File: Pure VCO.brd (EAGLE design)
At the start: 48.8 x 100 mm, 76 parts, among them T1 TRANS_PAIR, T2 N_CHN, U1 QUAD_OPAMP, U2 QUAD_OPAMP, U3 DUAL_OPAMP

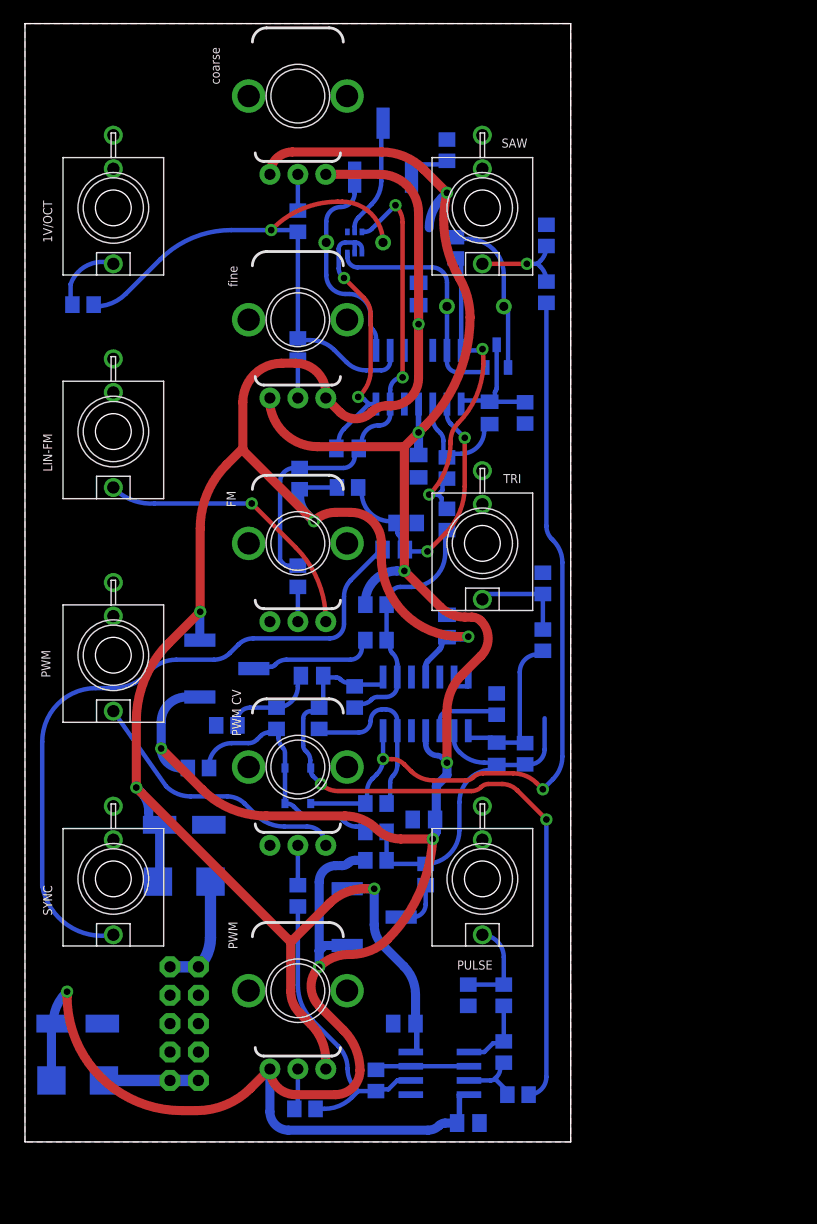
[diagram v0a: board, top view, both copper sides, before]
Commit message: VCO 2.1
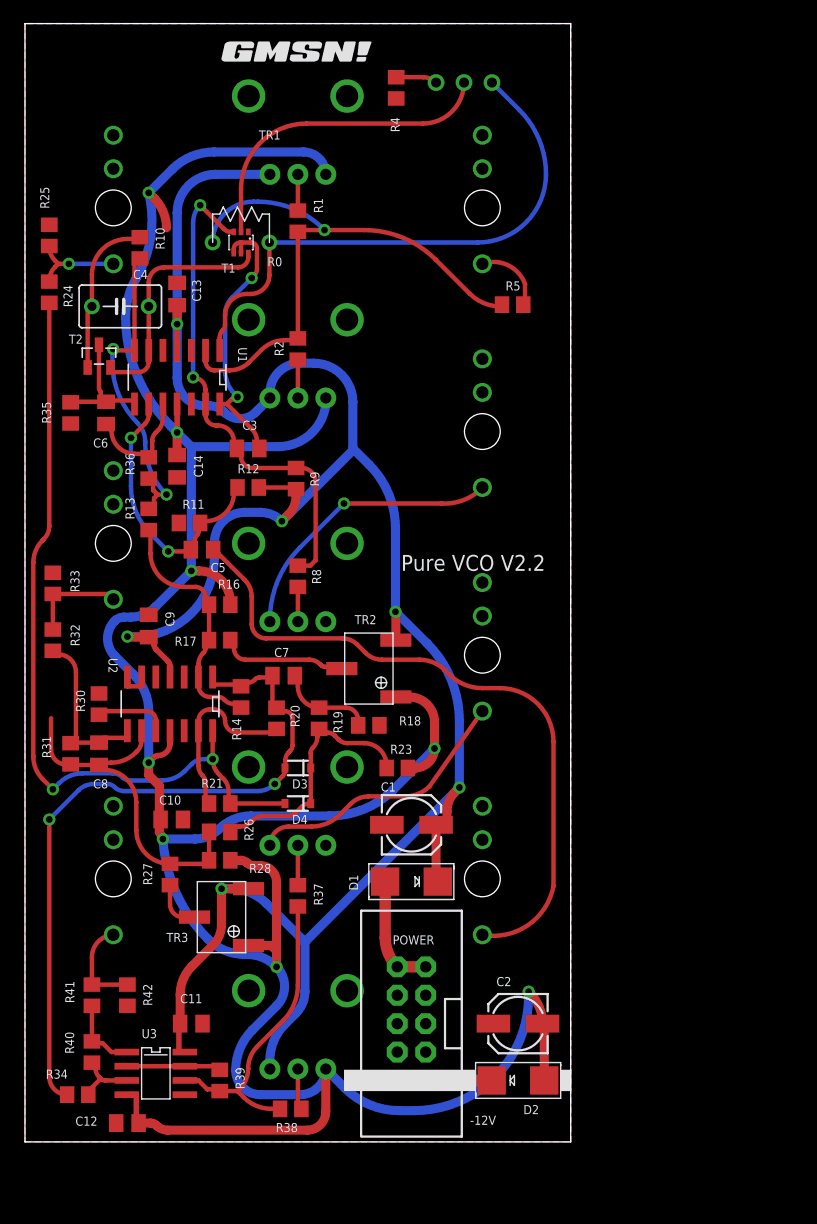
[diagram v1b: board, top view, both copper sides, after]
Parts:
- removed 2M, 2M1, 2M4, 2M5: 2K2, rcl:R0805
- removed 2M3: 120K, rcl:R0805
- removed 3K1: 9K1, rcl:R0805
- removed 3K3: 15K, rcl:R0805
- added R35, R41: 3K3, rcl:R0805
- added R36: 9K1, rcl:R0805
- added R38: 120K, rcl:R0805
- added R39: 100K, rcl:R0805
- added R40: 2M, rcl:R0805
- added R42: 1K5, rcl:R0805
- added U$1, U$2: (no value), gmsnLogo:GMSN!_LOGO
- R23: value 19K -> 19k1
- TR1: device INSTRUO:TRIM_3269W -> INSTRUO:TRIMMER_TH3
- moved R24 44.5 mm to (3.17, 92.7), flipped to the top
- moved R25 44.5 mm to (3.17, 97.8), flipped to the top
- moved R32 43.8 mm to (3.49, 61.6), flipped to the top
- moved R33 43.8 mm to (3.49, 66.7), flipped to the top
- moved R31 40.6 mm to (5.08, 51.4), flipped to the top
- moved C2 39.4 mm to (45.1, 27.3), flipped to the top
- moved D2 39.4 mm to (45.1, 22.2), flipped to the top
- moved R34 39.4 mm to (5.71, 21.0), flipped to the top
- moved R5 38.4 mm to (44.6, 91.6), flipped to the top
- moved C8 35.6 mm to (7.62, 51.4), flipped to the top
- moved R30 35.6 mm to (7.62, 55.9), flipped to the top
- moved T2 35.6 mm to (7.62, 87.0), flipped to the top
- moved C6 34.3 mm to (8.26, 81.9), flipped to the top
- moved 1V/OCT 33.0 mm to (41.9, 100.2), flipped to the bottom
- moved LIN-FM 33.0 mm to (41.9, 80.2), flipped to the bottom
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- renumbered 2M2 to R37
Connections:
- net GND: now also R35.1, R42.1; no longer 2M5.1, 3K3.1
- net N$16: now also R36.2; no longer 3K1.2
- net N$19: now also R36.1; no longer 3K1.1
- net N$20: now also R35.2; no longer 3K3.2
- net N$36: now also R40.1; no longer 2M.1
- net N$39: now also R40.2, R41.2; no longer 2M.2, 2M4.2
- net N$40: now also R38.1; no longer 2M3.1
- net N$42: now also R38.2, R39.1; no longer 2M1.1, 2M3.2
- net N$43: now also R39.2; no longer 2M1.2
- net N$44: now also R41.1, R42.2; no longer 2M4.1, 2M5.2
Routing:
- net N$7: track 18.5 -> 48.5 mm
- net N$10: track 10.5 -> 27.7 mm
- net N$8: track 4.36 -> 3.66 mm
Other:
- board text added: "Pure VCO V2.2"
- board text added: "copyright GMSN Ltd 2016"

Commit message: VCO 2.3
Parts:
- removed 1V/OCT, LIN-FM, PULSE, PWM, SAW, SYNC, TRI: (no value), INSTRUO:S_JACK
- removed COARSE, FINE, FM_ATT, PWM_ATT, PWM_POT: B100K, INSTRUO:Q-POT
- removed R0: 2K, INSTRUO:RESISTOR_TC
- removed T2: N_CHN, INSTRUO:N_CHN
- removed U2: QUAD_OPAMP, INSTRUO:QUAD_OPAMP
- removed U3: DUAL_OPAMP, INSTRUO:DUAL_OPAMP
- added C15, C16, C18, C19: 100n, GMSN:C0805K
- added C17: 100p, GMSN:C0805K
- added CP1, CP2: 10u, GMSN:153CLV-0505
- added IC1, IC2, IC3, IC4, IC5, IC6: TL072D, GMSN:SO08
- added J1, J2, J3, J4, J5, J6, J7, J8: S_JACK, GMSN:S_JACK
- added R15: 56K, GMSN:R0805
- added R22: 1K5, GMSN:R0805
- added R29: 2K, GMSN:R0805
- added R3: 100K, GMSN:R0805
- added R43, R44, R46: 10K, GMSN:R0805
- added R45: empty, GMSN:R0805
- added R47: 1K3, GMSN:R0805
- added R6: 390R, GMSN:R0805
- added R7: 87k, GMSN:R0805
- added TC1: 2K, GMSN:RESISTOR_TC
- added TP1, TP2: TRANS_PAIR, GMSN:TRANS_PAIR
- added TR4, TR5: 100K, GMSN:TRIMMER_TH3
- added VR1: Coarse, GMSN:POT
- added VR2, VR3, VR4, VR5: B100K, GMSN:POT
- C1, C2: value (none) -> 100n; device rcl:153CLV-0505 -> GMSN:C0805K
- C10, C11, C12, C3, C9: device rcl:C0805K -> GMSN:C0805K
- C13: value 100n -> 10nF; device rcl:C0805K -> GMSN:C0805K
- C14: value 100n -> 1000p; device rcl:C0805K -> GMSN:C0805K
- C4: value 2.2n -> 100p; device INSTRUO:POLY_CAP -> GMSN:C0805K
- C5: value 100p -> 100n; device rcl:C0805K -> GMSN:C0805K
- C6: value 22p -> 100n; device rcl:C0805K -> GMSN:C0805K
- C7: value 10nF -> 2.2n; device rcl:C0805K -> GMSN:POLY_CAP
- C8: value 1000p -> 22p; device rcl:C0805K -> GMSN:C0805K
- D1, D2: device adafruit:SMADIODE -> GMSN:SMADIODE
- D3, D4: device SparkFun-DiscreteSemi:SOD-323 -> GMSN:SOD-323F
- R1, R2: device rcl:R0805 -> GMSN:R0805
- R10: value 680R -> 39K; device rcl:R0805 -> GMSN:R0805
- R11: value 15K -> 680R; device rcl:R0805 -> GMSN:R0805
- R12: value 22K -> 9K1; device rcl:R0805 -> GMSN:R0805
- R13: value 10K -> 5K6; device rcl:R0805 -> GMSN:R0805
- R14: value 39K -> 10K; device rcl:R0805 -> GMSN:R0805
- R16: value 56K -> 100K; device rcl:R0805 -> GMSN:R0805
- R17: value 5K6 -> 39K; device rcl:R0805 -> GMSN:R0805
- R18: value 10K -> 2K2; device rcl:R0805 -> GMSN:R0805
- R19: value 10K -> 2M; device rcl:R0805 -> GMSN:R0805
- R20: value 22K* -> 10K; device rcl:R0805 -> GMSN:R0805
- R21: value 22K* -> 3K3; device rcl:R0805 -> GMSN:R0805
- R23: value 19k1 -> 10K; device rcl:R0805 -> GMSN:R0805
- R24, R25: value 2K -> 22K*; device rcl:R0805 -> GMSN:R0805
- R26: value 10K -> 19k1; device rcl:R0805 -> GMSN:R0805
- R27: value 100K -> 2K; device rcl:R0805 -> GMSN:R0805
- R28: value 27K -> 10K; device rcl:R0805 -> GMSN:R0805
- R30: value * -> 100K; device rcl:R0805 -> GMSN:R0805
- R31: value 10K -> 27K; device rcl:R0805 -> GMSN:R0805
- R32: value 1K3 -> 10K; device rcl:R0805 -> GMSN:R0805
- R33: value 2K -> 1K3; device rcl:R0805 -> GMSN:R0805
- R34: value 2K2 -> 2K; device rcl:R0805 -> GMSN:R0805
- R35: value 3K3 -> 1K3; device rcl:R0805 -> GMSN:R0805
- R36: value 9K1 -> 3K3; device rcl:R0805 -> GMSN:R0805
- R37: value 39K -> 2K; device rcl:R0805 -> GMSN:R0805
- R38: value 120K -> 10K; device rcl:R0805 -> GMSN:R0805
- R39: value 100K -> 402R; device rcl:R0805 -> GMSN:R0805
- R4: value 390R -> 2M; device rcl:R0805 -> GMSN:R0805
- R40: value 2M -> 10K; device rcl:R0805 -> GMSN:R0805
- R41: value 3K3 -> 10K; device rcl:R0805 -> GMSN:R0805
- R42: value 1K5 -> 2K; device rcl:R0805 -> GMSN:R0805
- R5: value 100K -> 560K; device rcl:R0805 -> GMSN:R0805
- R8: value 560K -> 3K3; device rcl:R0805 -> GMSN:R0805
- R9: value 2M -> 120K; device rcl:R0805 -> GMSN:R0805
- T1: value TRANS_PAIR -> N_CHN; device INSTRUO:TRANS_PAIR -> GMSN:N_CHN
- TR1: device INSTRUO:TRIMMER_TH3 -> GMSN:TRIMMER_TH3
- TR2, TR3: device INSTRUO:TRIM_3269W -> GMSN:TRIMMER_TH3
- U1: value QUAD_OPAMP -> LM4040A50IDBZT; device INSTRUO:QUAD_OPAMP -> GMSN:SOT95P237X112-3N
- moved U$1 95.7 mm to (41.1, 19.7)
- moved C2 75.2 mm to (15.4, 96.4)
- moved C12 65.3 mm to (11.2, 83.7)
- moved C1 64.3 mm to (5.08, 101.7), turned to 180 degrees
- moved C8 62.1 mm to (46.7, 99.7)
- moved R10 53.1 mm to (26.0, 45.7), turned to 0 degrees
- moved R9 50.0 mm to (24.8, 26.0), turned to 180 degrees
- moved C11 48.5 mm to (7.87, 75.2)
- moved C10 47.6 mm to (42.4, 83.9), turned to 0 degrees
- moved C4 47.3 mm to (37.8, 53.5), turned to 0 degrees
- moved R8 42.9 mm to (46.6, 104.6), turned to 180 degrees
- moved C5 42.5 mm to (41.5, 104.3)
- moved R27 41.4 mm to (3.43, 80.6), turned to 180 degrees
- moved C7 40.5 mm to (39.6, 95.9), flipped to the bottom, turned to 180 degrees
- moved D2 37.1 mm to (30.4, 56.3), turned to 90 degrees
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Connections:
- removed net N$25: C7.1, D3.2, R14.1, R20.2, R34.1, U2.1OUT
- removed net N$35: R30.2, U2.3+IN
- removed net N$38: R32.1, R33.1, TRI.TIP
- removed net N$43: R39.2, U3.-1IN, U3.2OUT
- removed net N$45: U2.2-IN, U2.2OUT
- new net N$14: C17.1, IC6.2, R38.2, R44.2, TP2.C2
- new net N$6: IC3.1, IC3.6, R16.2
- new net N$75: IC5.7, R47.1, TR4.1, TR4.2
- new net N$76: R37.1, TP2.B2, TR4.3
- new net N$77: R39.1, TP2.E2, TR5.1
- new net N$78: R39.2, TP2.E1, TR5.3
- new net N$79: R40.1, TR5.2
- new net N$80: R42.1, TP2.B1
- new net N$82: IC6.3, R41.2, R43.1, TP2.C1
- new net N$83: IC5.5, R35.1, R36.1
- new net N$84: IC6.6, R45.2, R46.2
- new net PULSEIN: C13.1, D3.A, IC4.1, R17.1, R18.1, R24.2
- new net SAWCORE: IC2.1, R11.1, R12.1, R14.2
- new net SINE: IC6.7, J8.TIP, R46.1
- new net SINE_PRE1: C17.2, IC6.1, IC6.5, R44.1
- new net TRI: J7.TIP, R33.1, R34.1, R35.2
- net +12V: now also C1.1, C15.1, C18.1, C5.1, CP1.+, IC1.8, IC2.8, IC3.8, IC4.8, IC5.8, IC6.8, R38.1, R4.2, R41.1, R7.2, VR1.P$3, VR2.P$3, VR4.P$3; no longer C1.+, C13.1, COARSE.P$3, FINE.P$3, PWM_POT.P$3, R12.2, R9.2, U1.VCC++, U2.VCC++, U3.+VCC
- net -12V: now also C16.2, C19.2, C2.2, C6.2, CP2.-, IC1.4, IC2.4, IC3.4, IC4.4, IC5.4, IC6.4, R15.2, R26.2, R31.1, R40.2, VR1.P$1, VR2.P$1, VR4.P$1; no longer C14.2, C2.-, COARSE.P$1, FINE.P$1, PWM_POT.P$1, R16.2, R23.2, R28.1, U1.VCC--, U2.VCC--, U3.-VCC
- net GND: now also C1.2, C15.2, C16.1, C18.2, C19.1, C2.1, C5.2, C6.1, CP1.-, CP2.+, IC1.3, IC1.5, IC2.3, IC3.3, IC4.3, IC4.5, IC5.3, J1.GND, J1.NORM, J2.GND, J2.NORM, J3.GND, J4.GND, J5.GND, J6.GND, J7.GND, J8.GND, R20.2, R22.1, R29.2, R34.2, R36.2, R37.2, R42.2, R43.2, R45.1, R6.1, R8.1, TP1.B1, U1.2, VR3.P$1, VR5.P$1; no longer 1V/OCT.GND, 1V/OCT.NORM, C1.-, C13.2, C14.1, C2.+, FM_ATT.P$1, LIN-FM.GND, LIN-FM.NORM, PULSE.GND, PWM.GND, PWM_ATT.P$1, R11.1, R18.2, R25.2, R30.1, R33.2, R35.1, R4.1, R42.1, SAW.GND, SYNC.GND, T1.B2, TRI.GND, U1.1+IN, U1.2+IN, U1.4+IN, U2.1+IN, U2.2+IN, U2.4+IN, U3.+2IN
- net N$10: now also TP1.B2; no longer T1.B1
- net N$11: now also C7.2, R11.2, T1.D; no longer C4.2, R10.2, T2.D
- net N$12: now also IC1.6, R4.1, R5.1, TP1.C2; no longer R8.1, R9.1, T1.C1, U1.4-IN
- net N$13: now also C7.1, IC2.2, T1.S, TP1.C1; no longer C4.1, T1.C2, T2.S, U1.2-IN
- net N$15: now also J1.TIP, VR3.P$3; no longer FM_ATT.P$3, LIN-FM.TIP
- net N$16: now also C8.1, IC2.5, R12.2; no longer C6.1, R36.2, U1.3+IN
- net N$17: now also R5.2, VR3.P$2; no longer FM_ATT.P$2, R8.2
- net N$18: now also IC1.7, TP1.E1, TP1.E2; no longer T1.E1, T1.E2, U1.4OUT
- net N$19: now also IC5.6, R47.2; no longer R10.1, R13.2, R36.1, U1.2OUT
- net N$2: now also VR1.P$2; no longer COARSE.P$2
- net N$20: now also C8.2, IC2.7, R8.2, T1.G; no longer C6.2, R35.2, T2.G, U1.3OUT
- net N$21: now also C4.1, J3.TIP; no longer C5.1, SYNC.TIP
- net N$22: now also C4.2, IC2.6, R7.1, U1.1; no longer C5.2, R11.2, R12.1, U1.3-IN
- net N$23: now also R13.1; no longer R17.1
- net N$24: now also IC4.2, R13.2, R14.1, R15.1; no longer R13.1, R14.2, R16.1, U2.1-IN
- net N$27: now also J6.TIP, R27.1, R29.1; no longer R24.1, R25.1, SAW.TIP
- net N$28: now also C13.2, R20.1, R23.1; no longer C7.2, R18.1, R19.1
- net N$29: now also R30.1; no longer R27.1
- net N$30: now also IC4.6, R24.1, R25.2; no longer R20.1, R21.2, U2.4-IN
- net N$31: now also D4.A, IC4.7, R25.1, R27.2; no longer D4.2, R21.1, R24.2, U2.4OUT
- net N$33: now also D3.C, D4.C, R23.2, R28.1; no longer D3.1, D4.1, R19.2, R23.1
- net N$34: now also C14.1, IC5.2, R30.2, R32.2; no longer C8.1, R26.2, R27.2, U2.3-IN
- net N$36: now also IC3.5, R18.2, R19.1; no longer R34.2, R40.1, U3.+1IN
- net N$37: now also C14.2, IC5.1, R32.1, R33.2; no longer C8.2, R31.1, R32.2, U2.3OUT
- net N$39: now also IC3.7, R19.2, R21.2; no longer R40.2, R41.2, U3.1OUT
- net N$4: now also IC1.2, R3.1, TC1.1; no longer R0.1, R5.1, U1.1-IN
- net N$40: now also R9.1, VR4.P$2; no longer PWM_POT.P$2, R38.1
- net N$41: now also J4.TIP, VR5.P$3; no longer PWM.TIP, PWM_ATT.P$3
- net N$42: now also IC3.2, R10.2, R16.1, R9.2; no longer R37.2, R38.2, R39.1, U3.-2IN
- net N$44: now also J5.TIP, R21.1, R22.2; no longer PULSE.TIP, R41.1, R42.2
- net N$46: now also R10.1, VR5.P$2; no longer PWM_ATT.P$2, R37.1
- net N$5: now also VR2.P$2; no longer FINE.P$2
- net N$7: now also IC1.1, TC1.2; no longer R0.2, U1.1OUT
- net N$8: now also R6.2; no longer R4.2
- net N$9: now also J2.TIP, R3.2; no longer 1V/OCT.TIP, R5.2
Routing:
- net +12V: track 199.5 -> 273.7 mm
- net N$25: track 64.5 -> 0.00 mm, vias 2 -> 0
- net N$31: track 71.5 -> 9.45 mm, vias 2 -> 0
- net N$21: track 59.2 -> 3.30 mm
- net N$42: track 27.5 -> 80.6 mm, vias 0 -> 2
- net N$14: track 0.00 -> 50.5 mm
- net N$75: track 0.00 -> 39.2 mm
- net PULSEIN: track 0.00 -> 37.6 mm
- net N$4: track 52.4 -> 84.4 mm, vias 1 -> 2
- net SAWCORE: track 0.00 -> 31.6 mm
- net N$22: track 24.2 -> 54.9 mm
- net N$13: track 21.5 -> 50.4 mm, vias 0 -> 1
- net -12V: track 259.0 -> 231.3 mm, vias 8 -> 7
- net N$82: track 0.00 -> 27.7 mm
- net N$7: track 48.5 -> 21.7 mm
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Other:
- board text added: "Pure VCO V3 cc-by 4.0 2017"
- board text removed: "-12V"
- board text removed: "FM"
- board text removed: "POWER"
- board text removed: "PWM"
- board text removed: "PWM CV"
- board text removed: "Pure VCO V2.2"
- board text removed: "T1"
- board text removed: "T2"
- board text removed: "TR1"
- board text removed: "TR2"
- board text removed: "TR3"
- board text removed: "coarse"
- board text removed: "copyright GMSN Ltd 2016"
- board text removed: "fine"

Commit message: VCO 3.0
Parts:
- removed J1, J2, J3, J4, J5, J6, J7, J8: S_JACK, GMSN:S_JACK
- removed U1: LM4040A50IDBZT, GMSN:SOT95P237X112-3N
- removed VR1: Coarse, GMSN:POT
- removed VR2, VR3, VR4, VR5: B100K, GMSN:POT
- added 1V/OCT, LIN, MIX, PULSE, PWM_IN, SAW, SINE, SYNC, TRI: PJ301M-12, GMSN:PJ301M-12
- added C20, C21: 100nF, GMSN:C0805
- added COARSE, FINE, FM_LEVEL, PULSE_MIX, PULSE_WIDTH, PWM_LEVEL, SAW_MIX, SINE_MIX, TRI_MIX: B100k, GMSN:POTENTIOMETER_9MM
- added IC7: TL072, GMSN:SO08
- added IC8: LM4040A50IDBZT, GMSN:SOT95P237X112-3N
- added R48, R49, R50, R51, R52, R53: 100k, GMSN:R0805
- C1, C10, C11, C12, C15, C16, C18, C19, C2, C5, C6, C9: value 100n -> 100nF; device GMSN:C0805K -> GMSN:C0805
- C13: device GMSN:C0805K -> GMSN:C0805
- C14: value 1000p -> 1nF; device GMSN:C0805K -> GMSN:C0805
- C17, C3, C4: value 100p -> 100pF; device GMSN:C0805K -> GMSN:C0805
- C7: value 2.2n -> 2.2nF
- C8: value 22p -> 22pF; device GMSN:C0805K -> GMSN:C0805
- CP1, CP2: value 10u -> 10uF
- D1, D2: value (none) -> STTH102A
- D3, D4: value (none) -> 1N914
- IC1, IC2, IC3, IC4, IC5, IC6: value TL072D -> TL072
- JP1: value M05X2SHD -> HEADER2X5SHD; device SparkFun-Connectors:2X5-SHROUDED -> GMSN:2X5-SHROUDED
- R1: value 150K -> 150k
- R10, R17: value 39K -> 39k
- R12: value 9K1 -> 9k1
- R13: value 5K6 -> 5k6
- R14, R20, R23, R28, R38, R40, R41, R43, R44: value 10K -> 10k
- R15: value 56K -> 56k
- R16, R3, R30: value 100K -> 100k
- R18: value 2K2 -> 2k2
- R21: value 3K3 -> 1k5
- R22: value 1K5 -> 1k5
- R24, R25: value 22K* -> 22k
- R27, R29, R34, R37, R42: value 2K -> 2k
- R31: value 27K -> 27k
- R32, R46: value 10K -> 19k1
- R33, R35, R47: value 1K3 -> 1k3
- R36, R8: value 3K3 -> 3k3
- R45: value empty -> 10k
- R5: value 560K -> 560k
- R9: value 120K -> 120k
- T1: value N_CHN -> MMBFJ309
- TC1: value 2K -> 2k; device GMSN:RESISTOR_TC -> GMSN:0204/7
- TP1, TP2: value TRANS_PAIR -> DMMT3904W-7-F
- TR1: device GMSN:TRIMMER_TH3 -> GMSN:TRIMMER_TH
- TR2, TR3, TR4, TR5: value 100K -> 100k; device GMSN:TRIMMER_TH3 -> GMSN:TRIMMER_TH
- moved U$1 68.9 mm to (51.5, 87.8), turned to 90 degrees
- moved R36 50.2 mm to (52.8, 54.1), turned to 0 degrees
- moved TR3 50.1 mm to (55.9, 57.8)
- moved R30 47.8 mm to (58.4, 39.2), turned to 270 degrees
- moved R47 47.7 mm to (52.5, 51.7), turned to 0 degrees
- moved C16 46.5 mm to (56.0, 43.8), turned to 270 degrees
- moved D1 46.5 mm to (50.8, 14.0), turned to 180 degrees
- moved R35 45.3 mm to (48.1, 54.1), turned to 180 degrees
- moved C4 45.0 mm to (67.0, 19.2)
- moved CP2 44.9 mm to (20.3, 19.1), turned to 0 degrees
- moved R31 44.5 mm to (56.1, 39.0), turned to 270 degrees
- moved D2 43.5 mm to (20.3, 14.0), turned to 180 degrees
- moved R44 43.4 mm to (18.5, 61.3)
- moved IC5 43.1 mm to (52.2, 46.2), turned to 0 degrees
- moved CP1 42.7 mm to (50.8, 19.1), turned to 0 degrees
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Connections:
- removed net N$27: J6.TIP, R27.1, R29.1
- new net N$25: IC7.6, IC7.7
- new net N$35: IC7.3, R48.2, R49.2, R50.2, R51.2
- new net N$38: R48.1, SAW_MIX.P$2
- new net N$43: R49.1, TRI_MIX.P$2
- new net N$45: R51.1, SINE_MIX.P$2
- new net N$48: IC7.2, R52.1, R53.2
- new net N$49: IC7.1, MIX.TIP, R52.2
- new net PULSE: PULSE.TIP, PULSE_MIX.P$3, R21.1, R22.2
- new net SAW: R27.1, R29.1, SAW.TIP, SAW_MIX.P$3
- net +12V: now also C20.1, COARSE.P$3, FINE.P$3, IC7.8, PULSE_WIDTH.P$3; no longer VR1.P$3, VR2.P$3, VR4.P$3
- net -12V: now also C21.2, COARSE.P$1, FINE.P$1, IC7.4, PULSE_WIDTH.P$1; no longer VR1.P$1, VR2.P$1, VR4.P$1
- net GND: now also 1V/OCT.GND, 1V/OCT.NORM, C20.2, C21.1, FM_LEVEL.P$1, IC7.5, IC8.2, LIN.GND, LIN.NORM, MIX.GND, PULSE.GND, PULSE_MIX.P$1, PWM_IN.GND, PWM_LEVEL.P$1, R53.1, SAW.GND, SAW_MIX.P$1, SINE.GND, SINE_MIX.P$1, SYNC.GND, TRI.GND, TRI_MIX.P$1; no longer J1.GND, J1.NORM, J2.GND, J2.NORM, J3.GND, J4.GND, J5.GND, J6.GND, J7.GND, J8.GND, U1.2, VR3.P$1, VR5.P$1
- net N$15: now also FM_LEVEL.P$3, LIN.TIP; no longer J1.TIP, VR3.P$3
- net N$17: now also FM_LEVEL.P$2; no longer VR3.P$2
- net N$2: now also COARSE.P$2; no longer VR1.P$2
- net N$21: now also SYNC.TIP; no longer J3.TIP
- net N$22: now also IC8.1; no longer U1.1
- net N$40: now also PULSE_WIDTH.P$2; no longer VR4.P$2
- net N$41: now also PWM_IN.TIP, PWM_LEVEL.P$3; no longer J4.TIP, VR5.P$3
- net N$44: now also PULSE_MIX.P$2, R50.1; no longer J5.TIP, R21.1, R22.2
- net N$46: now also PWM_LEVEL.P$2; no longer VR5.P$2
- net N$5: now also FINE.P$2; no longer VR2.P$2
- net N$9: now also 1V/OCT.TIP; no longer J2.TIP
- net SINE: now also SINE.TIP, SINE_MIX.P$3; no longer J8.TIP
- net TRI: now also TRI.TIP, TRI_MIX.P$3; no longer J7.TIP
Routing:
- net SAW: track 0.00 -> 146.8 mm
- net N$22: track 54.9 -> 159.9 mm
- net N$34: track 31.7 -> 108.8 mm
- net PULSE: track 0.00 -> 73.9 mm, vias 0 -> 1
- net N$35: track 0.00 -> 69.4 mm, vias 0 -> 4
- net -12V: track 231.3 -> 288.5 mm, vias 7 -> 9
- net +12V: track 273.7 -> 327.5 mm, vias 6 -> 12
- net N$49: track 0.00 -> 33.9 mm
- net SINE: track 11.6 -> 42.1 mm, vias 0 -> 2
- net N$10: track 7.35 -> 36.9 mm, vias 0 -> 2
- net N$44: track 24.9 -> 3.04 mm
- net TRI: track 17.8 -> 38.9 mm, vias 0 -> 1
- net N$3: track 30.9 -> 10.6 mm
- net N$42: track 80.6 -> 61.9 mm, vias 2 -> 0
- net N$4: track 84.4 -> 66.0 mm, vias 2 -> 0
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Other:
- board size 48.8 x 100 mm -> 68.8 x 100 mm
- board text added: "Pure VCO V3 cc-by 4.0 2018"
- board text removed: "Pure VCO V3 cc-by 4.0 2017"
